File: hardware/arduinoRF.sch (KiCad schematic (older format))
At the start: 130 parts

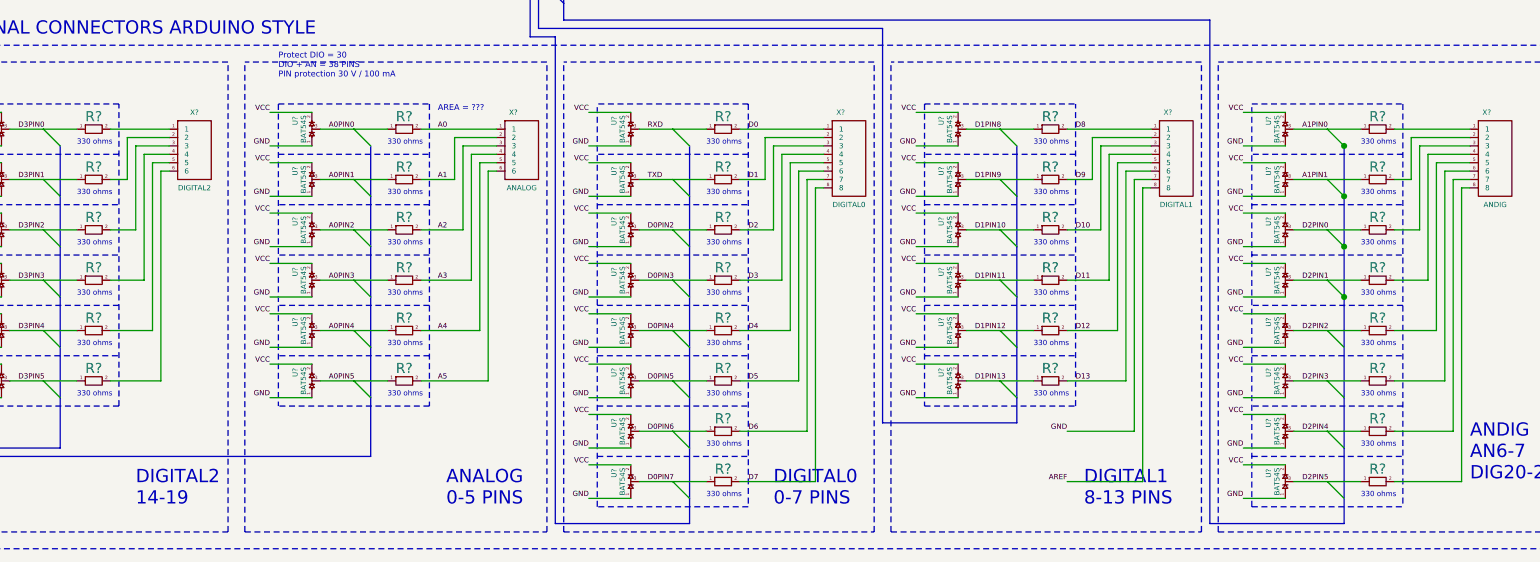
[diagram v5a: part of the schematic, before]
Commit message: Changes in schematic, board is modified and some lib files updated.
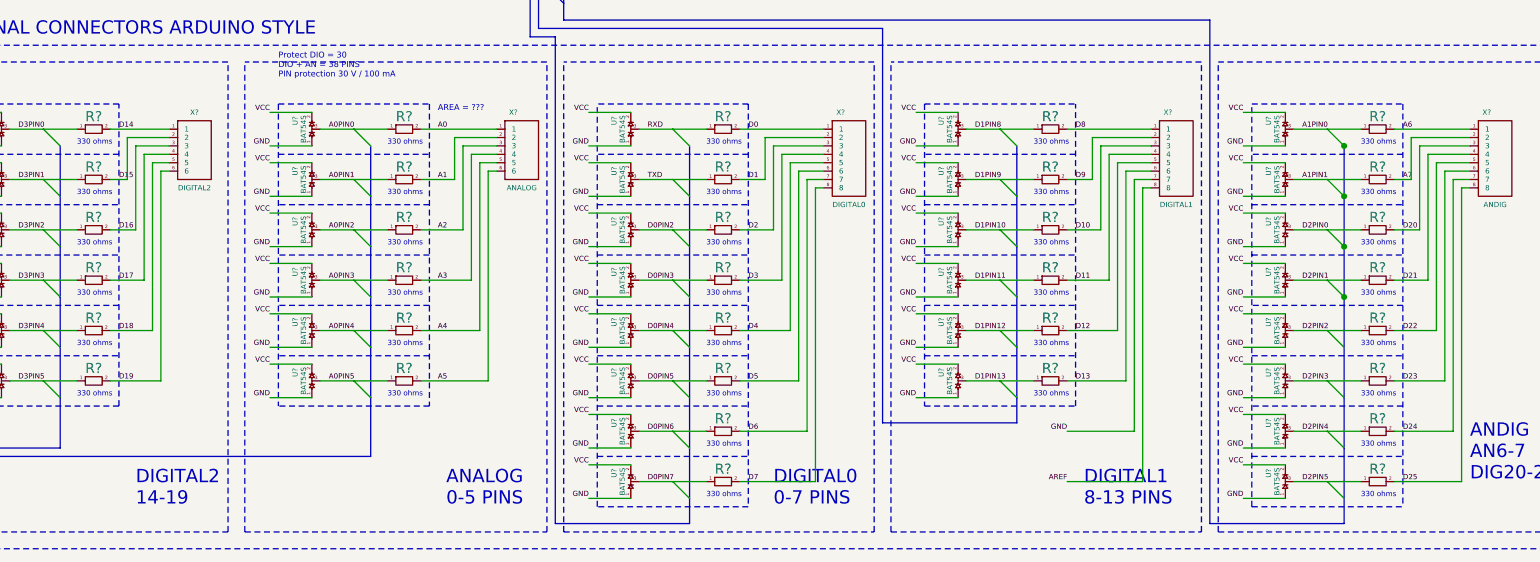
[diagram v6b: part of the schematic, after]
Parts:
- U?: footprint (none) -> crystal_xg6x3p5
- U?: footprint pin_strip_3x2 -> pin_array_3x2
- U?: footprint (none) -> pin_array_2x2
- X? (x3): footprint (none) -> arduinoRF_connector_6pins
- X? (x3): footprint (none) -> arduinoRF_connector_8pins
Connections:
- net A6: now reaches R?.2, X?.1
- net A7: now reaches R?.2, X?.2
- net D20: now reaches R?.2, X?.3
- net D21: now reaches R?.2, X?.4
- net D23: now reaches R?.2, X?.6
- net D22: now reaches R?.2, X?.5
- net D24: now reaches R?.2, X?.7
- net D25: now reaches R?.2, X?.8
- net D18: now reaches R?.2, X?.5
- net D19: now reaches R?.2, X?.6
- net D17: now reaches R?.2, X?.4
- net D16: now reaches R?.2, X?.3
- net D15: now reaches R?.2, X?.2
- net D14: now reaches R?.2, X?.1
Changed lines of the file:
@@
-EESchema Schematic File Version 2  date Fri 20 Apr 2012 02:53:01 PM EEST
+EESchema Schematic File Version 2  date Mon 23 Apr 2012 02:01:11 PM EEST
 LIBS:power
 LIBS:conn
@@
 Sheet 1 1
 Title "arduinoRF"
-Date "20 apr 2012"
+Date "23 apr 2012"
 Rev "1.0"
 Comp "rdrlab"
@@
 Comment4 ""
 $EndDescr
+Text Label 1900 9800 0    31   ~ 0
+D19
+Text Label 1900 9500 0    31   ~ 0
+D18
+Text Label 1900 9200 0    31   ~ 0
+D17
+Text Label 1900 8900 0    31   ~ 0
+D16
+Text Label 1900 8600 0    31   ~ 0
+D15
+Text Label 1900 8300 0    31   ~ 0
+D14
+Text Label 9550 10400 0    31   ~ 0
+D25
+Text Label 9550 10100 0    31   ~ 0
+D24
+Text Label 9550 9800 0    31   ~ 0
+D23
+Text Label 9550 9500 0    31   ~ 0
+D22
+Text Label 9550 9200 0    31   ~ 0
+D21
+Text Label 9550 8900 0    31   ~ 0
+D20
+Text Label 9550 8600 0    31   ~ 0
+A7
+Text Label 9550 8300 0    31   ~ 0
+A6
 Wire Wire Line
 	4200 5400 3200 5400
@@
 F 0 "X?" H 2350 8700 31  0000 C CNN
 F 1 "DIGITAL2" H 2350 8250 31  0000 C CNN
+F 2 "arduinoRF_connector_6pins" H 2350 8450 60  0001 C CNN
+F 3 "http://store.comet.bg/bg/Catalogue/Product/2997/" H 2350 8450 60  0001 C CNN
 	1    2350 8450
 	1    0    0    -1
@@
 F 0 "X?" H 10050 8800 31  0000 C CNN
 F 1 "ANDIG" H 10100 8250 31  0000 C CNN
+F 2 "arduinoRF_connector_8pins" H 10100 8500 60  0001 C CNN
+F 3 "http://store.comet.bg/bg/Catalogue/Product/2997/" H 10100 8500 60  0001 C CNN
 	1    10100 8500
 	1    0    0    -1
@@
 F 0 "X?" H 11300 8700 31  0000 C CNN
 F 1 "POWER" H 11300 8250 31  0000 C CNN
+F 2 "arduinoRF_connector_6pins" H 11300 8450 60  0001 C CNN
+F 3 "http://store.comet.bg/bg/Catalogue/Product/2997/" H 11300 8450 60  0001 C CNN
 	1    11300 8450
 	1    0    0    -1
@@
 F 0 "X?" H 8150 8800 31  0000 C CNN
 F 1 "DIGITAL1" H 8200 8250 31  0000 C CNN
+F 2 "arduinoRF_connector_8pins" H 8200 8500 60  0001 C CNN
+F 3 "http://store.comet.bg/bg/Catalogue/Product/2997/" H 8200 8500 60  0001 C CNN
 	1    8200 8500
 	1    0    0    -1
@@
 F 0 "X?" H 6200 8800 31  0000 C CNN
 F 1 "DIGITAL0" H 6250 8250 31  0000 C CNN
+F 2 "arduinoRF_connector_8pins" H 6250 8500 60  0001 C CNN
+F 3 "http://store.comet.bg/bg/Catalogue/Product/2997/" H 6250 8500 60  0001 C CNN
 	1    6250 8500
 	1    0    0    -1
@@
 F 0 "X?" H 4250 8700 31  0000 C CNN
 F 1 "ANALOG" H 4300 8250 31  0000 C CNN
+F 2 "arduinoRF_connector_6pins" H 4300 8450 60  0001 C CNN
+F 3 "http://store.comet.bg/bg/Catalogue/Product/2997/" H 4300 8450 60  0001 C CNN
 	1    4300 8450
 	1    0    0    -1
@@
 F 0 "U?" H 3500 4450 60  0000 C CNN
 F 1 "SPI" H 3500 4850 60  0000 C CNN
+F 2 "pin_array_2x2" H 3500 4650 60  0001 C CNN
 F 3 "pin_strip_3" H 3500 4650 60  0001 C CNN
 	1    3500 4650
@@
 F 0 "U?" H 4800 4350 60  0000 C CNN
 F 1 "ICSP" H 4850 4650 60  0000 C CNN
-F 2 "pin_strip_3x2" H 4850 4500 60  0001 C CNN
+F 2 "pin_array_3x2" H 4850 4500 60  0001 C CNN
 	1    4850 4500
 	1    0    0    -1
@@
 F 0 "U?" H 1400 5750 31  0000 C CNN
 F 1 "Q16.000" H 1350 5800 31  0000 C CNN
+F 2 "crystal_xg6x3p5" H 1350 5950 60  0001 C CNN
+F 3 "http://store.comet.bg/bg/Catalogue/Product/6270/" H 1350 5950 60  0001 C CNN
 	1    1350 5950
 	0    1    1    0

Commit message: Netlist and components list generated.
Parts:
- gave numbers to parts that had none: 129
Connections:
- net A1PIN2 is gone; now on net A1PIN1: U14.6 (PF7:ADC7:TDI)
- net VCC: now also C10.1
- net VIN: now also X9.6
- no-connect marks 9 -> 10

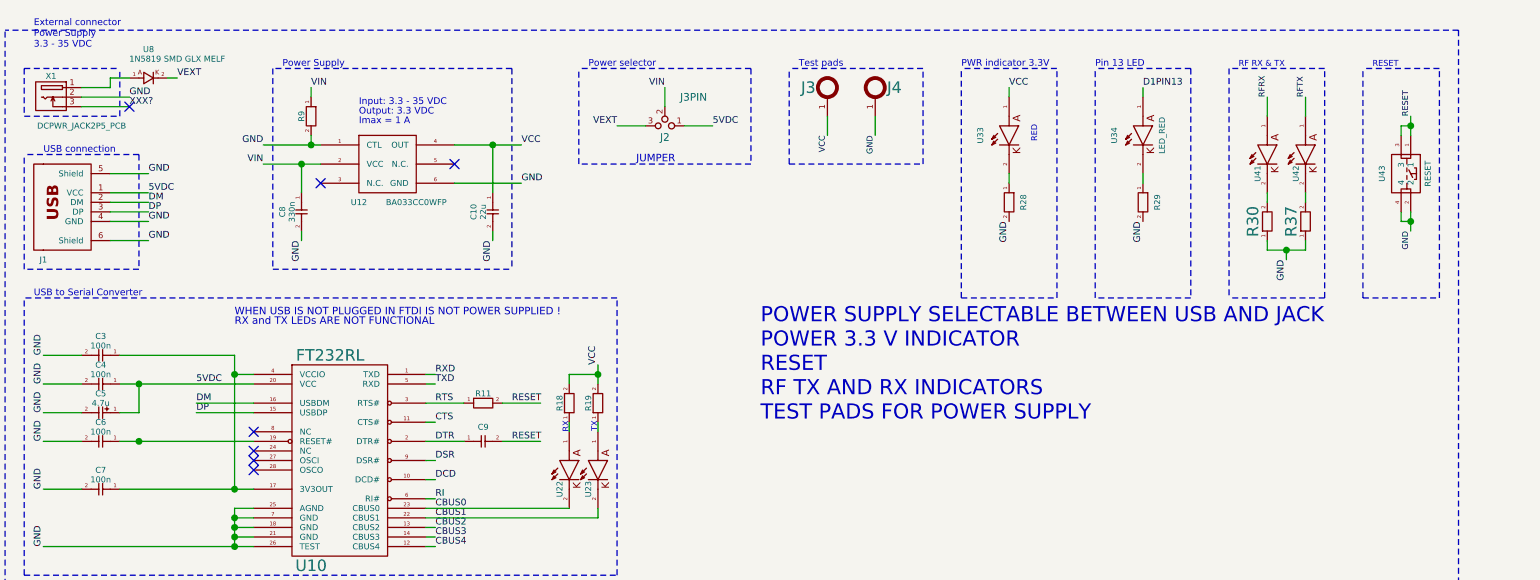
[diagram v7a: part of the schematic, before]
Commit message: Added test board to the project and the initial netlist.
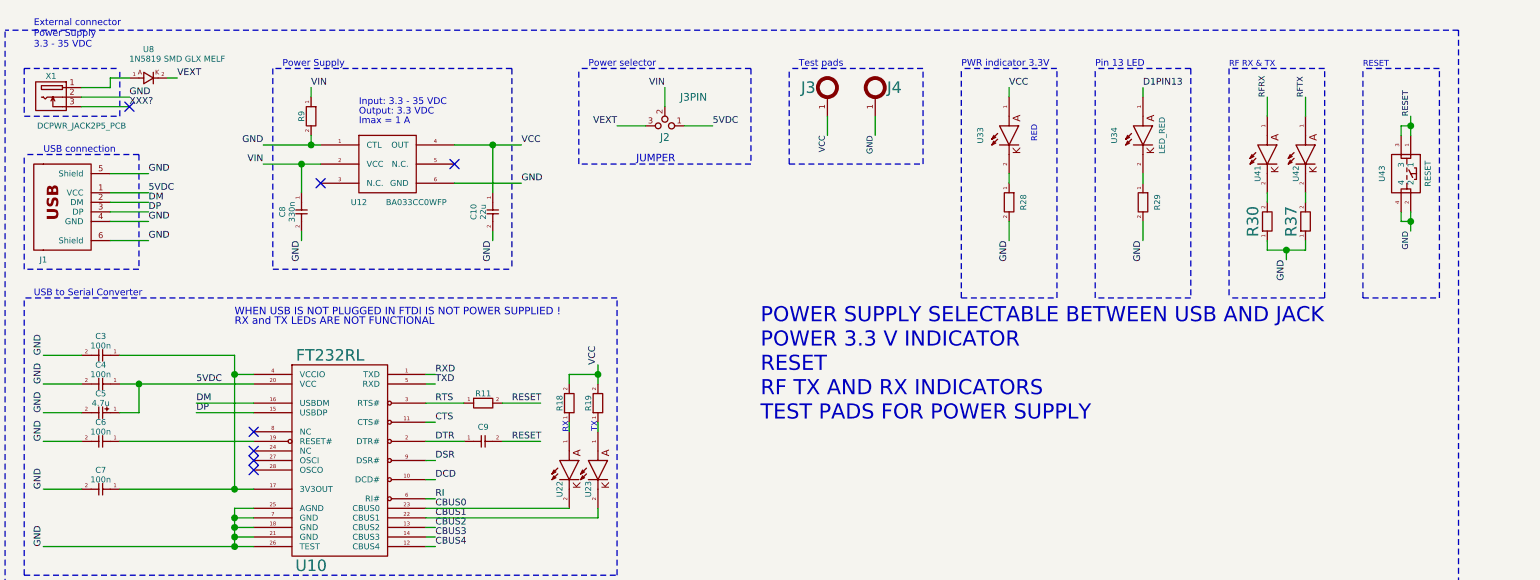
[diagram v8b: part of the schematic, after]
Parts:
- R28, R29, R30, R37: footprint (none) -> r_0603
- R9: value RES_0603 -> 10K
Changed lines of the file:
@@
-EESchema Schematic File Version 2  date Thu 26 Apr 2012 04:39:31 PM EEST
+EESchema Schematic File Version 2  date Thu 03 May 2012 02:19:20 PM EEST
 LIBS:power
 LIBS:conn
@@
 Sheet 1 1
 Title "arduinoRF"
-Date "26 apr 2012"
+Date "3 may 2012"
 Rev "1.0"
 Comp "rdrlab"
@@
 $EndDescr
 Wire Wire Line
+	6650 1800 6650 1900
+Wire Wire Line
 	11150 8550 11000 8550
 Wire Wire Line
@@
 Wire Wire Line
 	2900 2600 2950 2600
-Connection ~ 1400 2950
 Wire Wire Line
 	1300 3200 2000 3200
@@
 	3250 1650 3250 1400
 Connection ~ 3250 1400
+Wire Wire Line
+	5950 1800 5950 1900
 NoConn ~ 1350 1200
 Text Label 1900 9800 0    31   ~ 0
@@
 Text Notes 800  3950 0    79   ~ 0
 SUPPORTED INTERFACES: SERIAL(FTDI direct), ICSP, SPI, I2C
-Text Notes 7150 1000 0    31   ~ 0
+Text Notes 7100 1000 0    31   ~ 0
 RF RX & TX
 $Comp
@@
 Text Notes 3750 1000 0    35   ~ 0
 Power selector
-Text Label 6650 1800 3    35   ~ 0
+Text Label 6650 1900 3    35   ~ 0
 GND
-Text Label 5950 1800 3    35   ~ 0
+Text Label 5950 1900 3    35   ~ 0
 GND
 Text Notes 1900 2350 0    39   ~ 0
@@
 F 0 "R29" H 6650 1775 31  0000 C CNN
 F 1 "1K" H 6650 1800 31  0001 C CNN
+F 2 "r_0603" H 6650 1700 60  0001 C CNN
 	1    6650 1700
 	0    1    1    0
@@
 F 0 "R37" H 7500 1875 60  0000 C CNN
 F 1 "RES_0603" H 7500 1900 60  0001 C CNN
+F 2 "r_0603" H 7500 1800 60  0001 C CNN
 	1    7500 1800
 	0    -1   -1   0
@@
 F 0 "R30" H 7300 1875 60  0000 C CNN
 F 1 "RES_0603" H 7300 1900 60  0001 C CNN
+F 2 "r_0603" H 7300 1800 60  0001 C CNN
 	1    7300 1800
 	0    -1   -1   0
@@
 VCC
 NoConn ~ 2250 5950
-Text Notes 7850 1000 0    31   ~ 0
+Text Notes 7800 1000 0    31   ~ 0
 RESET
 Text Label 8050 1850 3    31   ~ 0
@@
 P 2300 1250
 F 0 "R9" H 2300 1200 31  0000 C CNN
-F 1 "RES_0603" H 2300 1350 60  0001 C CNN
+F 1 "10K" H 2300 1350 60  0001 C CNN
 F 2 "r_0603" H 2300 1250 60  0001 C CNN
 F 3 "http://store.comet.bg/bg/Catalogue/Product/4437/" H 2300 1250 60  0001 C CNN
@@
 F 0 "R28" H 5950 1775 31  0000 C CNN
 F 1 "1K" H 5950 1800 31  0001 C CNN
+F 2 "r_0603" H 5950 1700 60  0001 C CNN
 	1    5950 1700
 	0    1    1    0
